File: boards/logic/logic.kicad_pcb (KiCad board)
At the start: 2 copper layers, 48.3 x 76.2 mm, 41 parts, among them IC1 ATTINY85, P1 5V_IN, P2 PROG_CONN, P3 DSPLY_CONN, Q1 Q_NPN_EBC, Q2 Q_NPN_EBC, Q3 Q_NPN_EBC, Q4 Q_NPN_EBC, Q5 Q_NPN_EBC, Q6 Q_NPN_EBC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

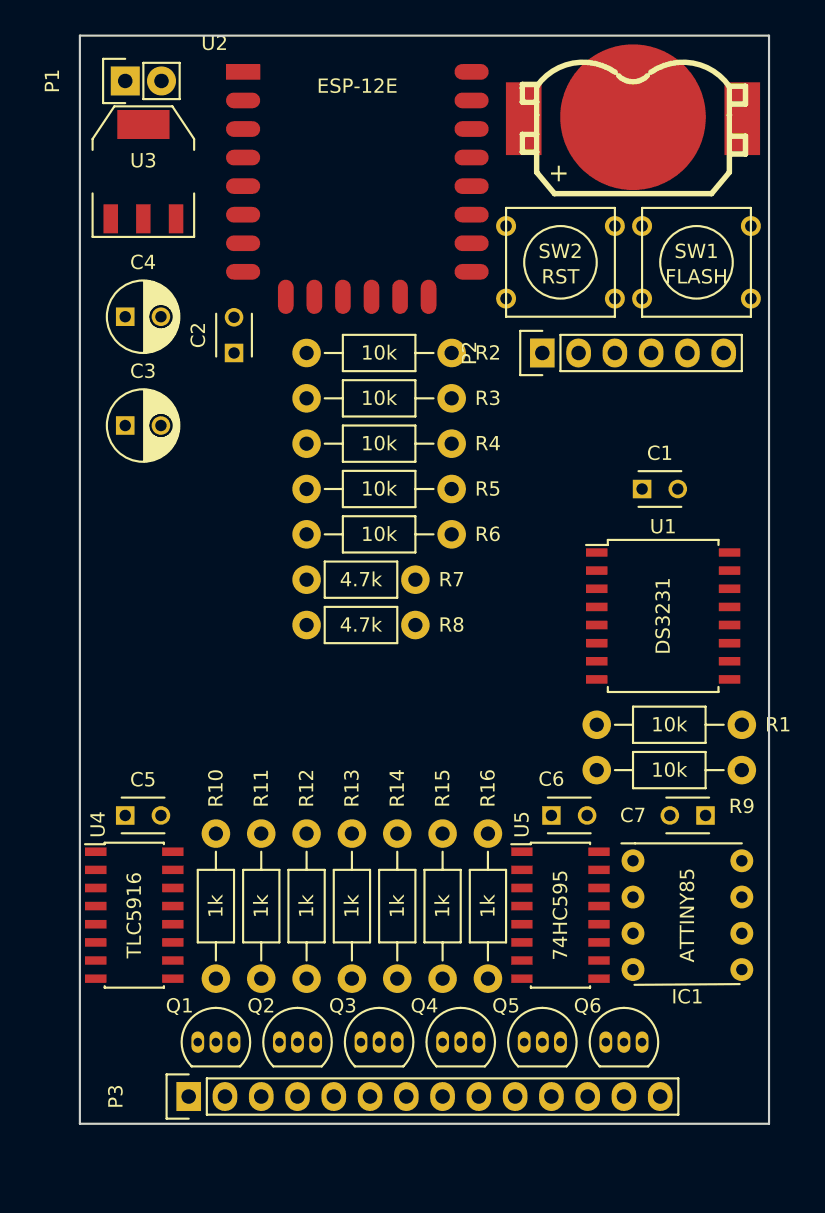
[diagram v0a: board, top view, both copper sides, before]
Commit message: Fit all the components into a smaller board footprint.
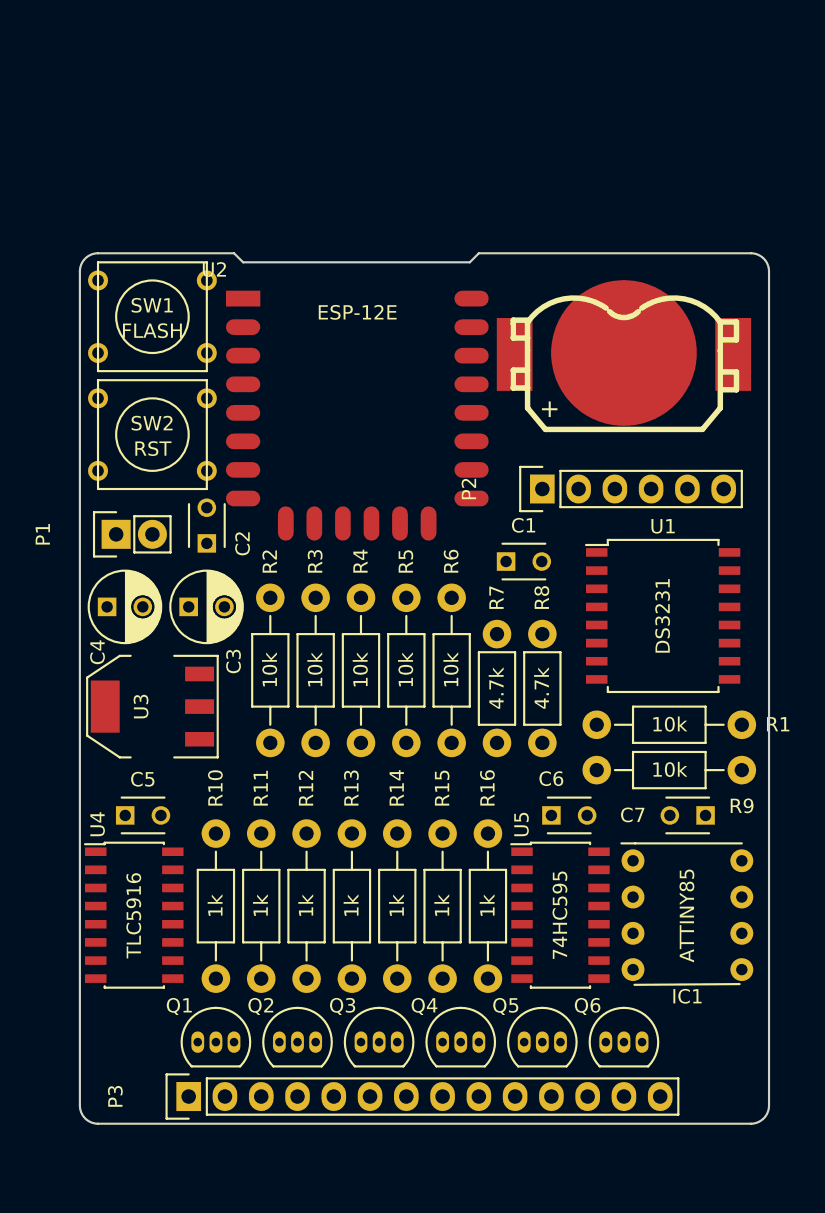
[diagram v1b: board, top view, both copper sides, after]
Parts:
- moved SW1 38.3 mm to (126.4, 87.6)
- moved U3 37.5 mm to (126.4, 114.9), turned to 90 degrees
- moved P1 31.8 mm to (123.8, 102.9)
- moved SW2 31.0 mm to (126.4, 95.9)
- moved R2 27.4 mm to (134.6, 117.5), turned to 90 degrees
- moved R3 24.1 mm to (137.8, 117.5), turned to 90 degrees
- moved R4 21.3 mm to (141.0, 117.5), turned to 90 degrees
- moved C4 20.4 mm to (123.2, 108.0)
- moved R5 19.1 mm to (144.1, 117.5), turned to 90 degrees
- moved R8 18.5 mm to (153.7, 117.5), turned to 90 degrees
- moved R6 17.8 mm to (147.3, 117.5), turned to 90 degrees
- moved R7 17.6 mm to (150.5, 117.5), turned to 90 degrees
- moved BT1 16.5 mm to (159.4, 90.2)
- moved U2 15.9 mm to (132.7, 86.4)
- moved C2 13.5 mm to (130.2, 103.5)
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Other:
- board size 48.3 x 76.2 mm -> 48.3 x 61 mm

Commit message: Switch the LM1117 footprint to SOT-223.
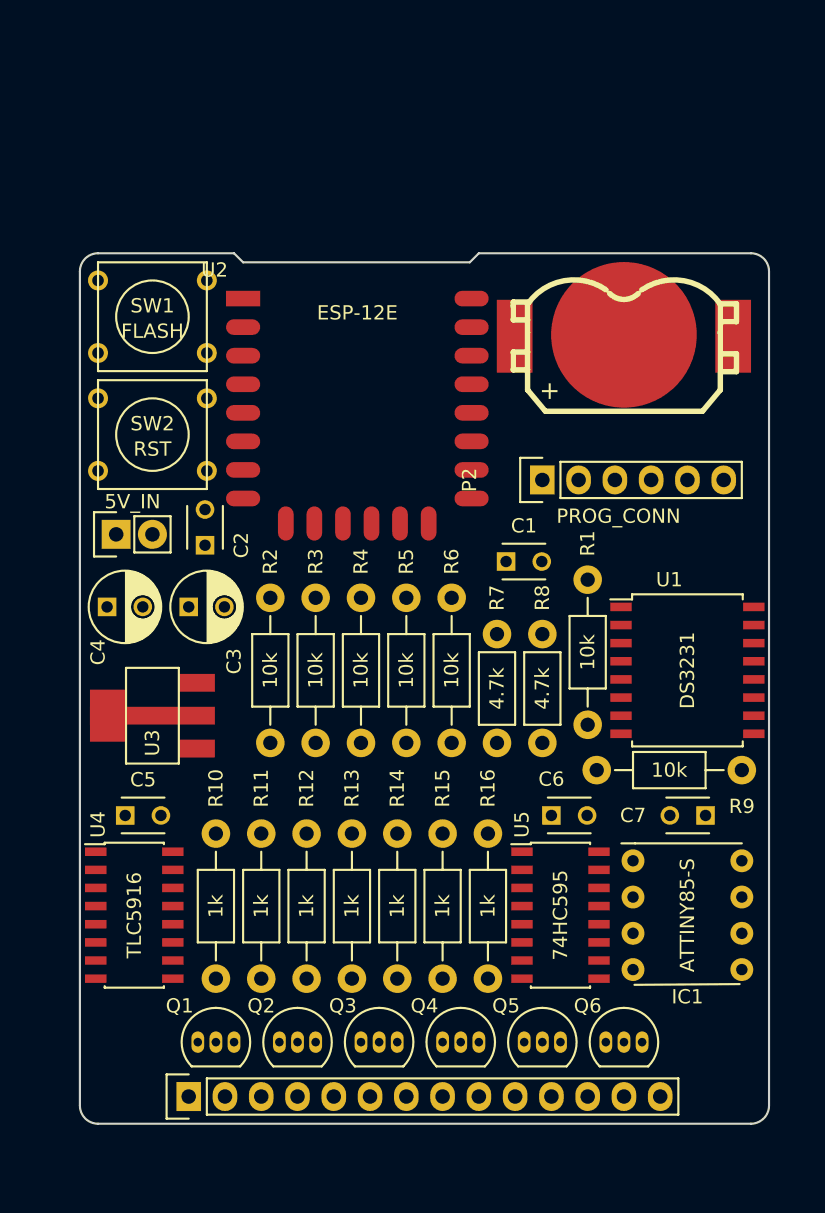
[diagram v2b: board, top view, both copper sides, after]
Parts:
- IC1: value ATTINY85 -> ATTINY85-S
- U3: footprint TO_SOT_Packages_SMD:SOT-223 -> myelin-kicad:SOT-223-LDO-1117LV
- moved U1 4.17 mm to (163.8, 112.4)
- moved BT1 1.27 mm to (159.4, 88.9)
- moved P2 0.63 mm to (153.7, 99.1)
- moved R1 0.63 mm to (156.8, 116.2), turned to 90 degrees
- moved U3 0.63 mm to (126.4, 115.6)
- moved C2 0.18 mm to (130.0, 103.6)

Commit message: Rearrange PCB layout to accomodate mounting screws.
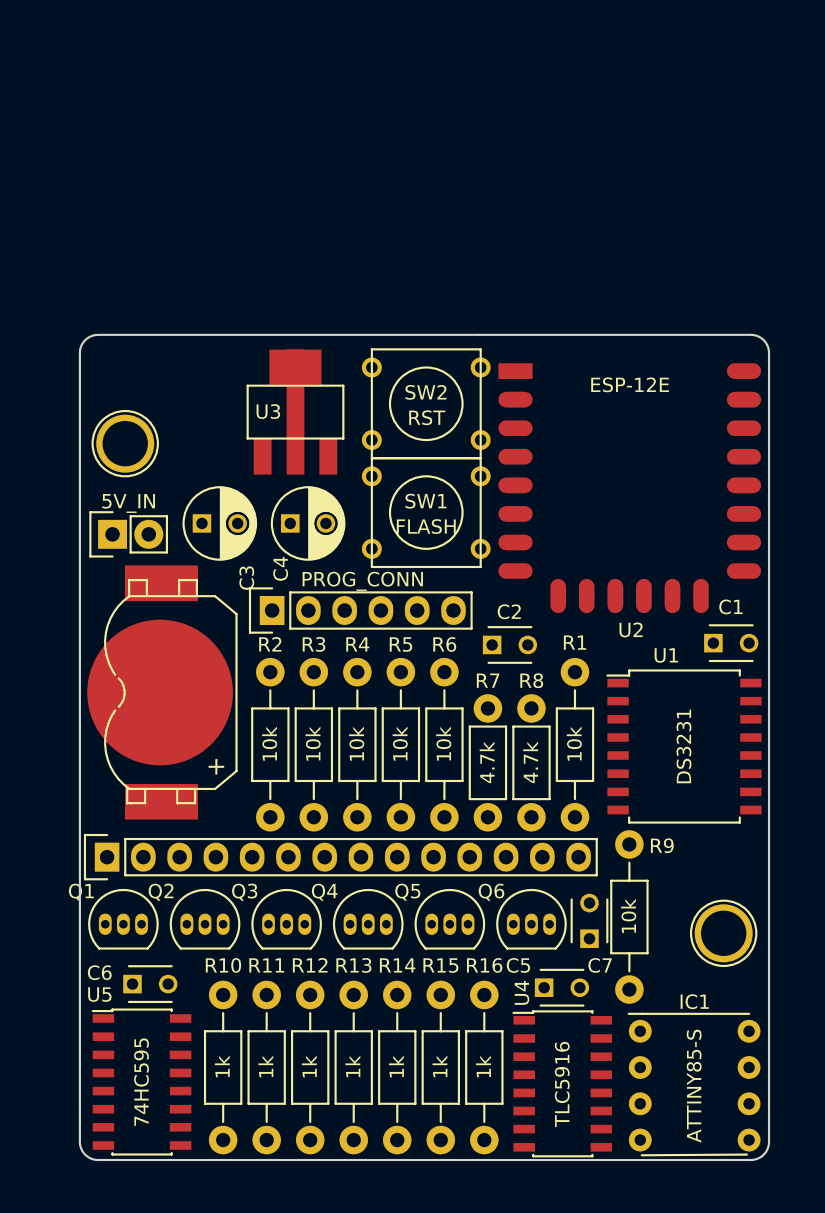
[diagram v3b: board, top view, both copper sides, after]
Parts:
- added REF**: 1pin, Connect:1pin, F.Cu at (166.4, 130.8)
- added REF**: 1pin, Connect:1pin, F.Cu at (124.5, 96.5)
- moved BT1 41.0 mm to (126.9, 113.9), turned to 270 degrees
- moved U4 32.2 mm to (155.1, 141.4)
- moved C5 31.7 mm to (153.8, 134.6)
- moved C6 31.6 mm to (125.0, 134.4)
- moved U5 31.5 mm to (125.6, 141.2)
- moved SW1 23.6 mm to (145.5, 101.3)
- moved U3 23.5 mm to (136.4, 94.3), turned to 0 degrees
- moved C2 21.3 mm to (150.2, 110.6), turned to 0 degrees
- moved P2 21.0 mm to (134.7, 108.2)
- moved U2 19.7 mm to (151.8, 91.4)
- moved SW2 19.3 mm to (145.5, 93.7)
- moved P3 17.7 mm to (123.2, 125.5)
- moved C1 15.6 mm to (165.6, 110.5)
- moved C4 14.1 mm to (136.0, 102.1)
- moved IC1 11.9 mm to (160.5, 137.7)
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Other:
- board size 48.3 x 61 mm -> 48.3 x 57.8 mm

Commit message: Add references for the mounting holes to allow spectra output to work.
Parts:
- renumbered REF** to REF1, REF** to REF2
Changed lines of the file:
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@@
     (links 117)
     (no_connects 116)
-    (area 121.209999 88.824999 169.620001 146.760001)
+    (area 97.104287 47.403566 203.751257 163.830001)
     (thickness 1.6)
     (drawings 29)
@@
     (descr "module 1 pin (ou trou mecanique de percage)")
     (tags DEV)
-    (fp_text reference REF** (at 0 -3.048) (layer F.SilkS) hide
+    (fp_text reference REF1 (at 0 -3.048) (layer F.SilkS) hide
       (effects (font (size 1 1) (thickness 0.15)))
     )
@@
     (descr "module 1 pin (ou trou mecanique de percage)")
     (tags DEV)
-    (fp_text reference REF** (at 0 -3.048) (layer F.SilkS) hide
-      (effects (font (size 1 1) (thickness 0.15)))
-    )
+    (fp_text reference REF2 (at 0 -3.048) (layer F.SilkS) hide
+      (effects (font (size 1 1) (thickness 0.15)))
+    )

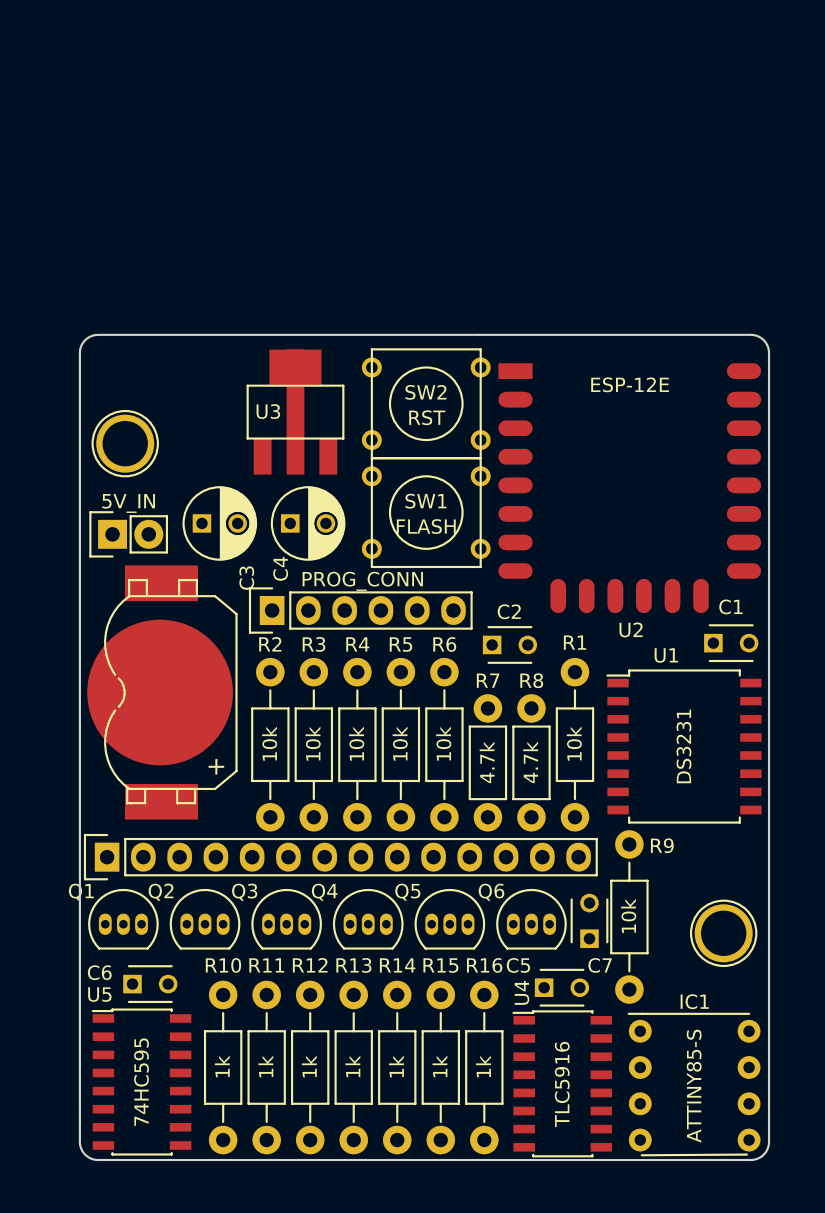
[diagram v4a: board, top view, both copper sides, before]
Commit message: Potential final board layout.
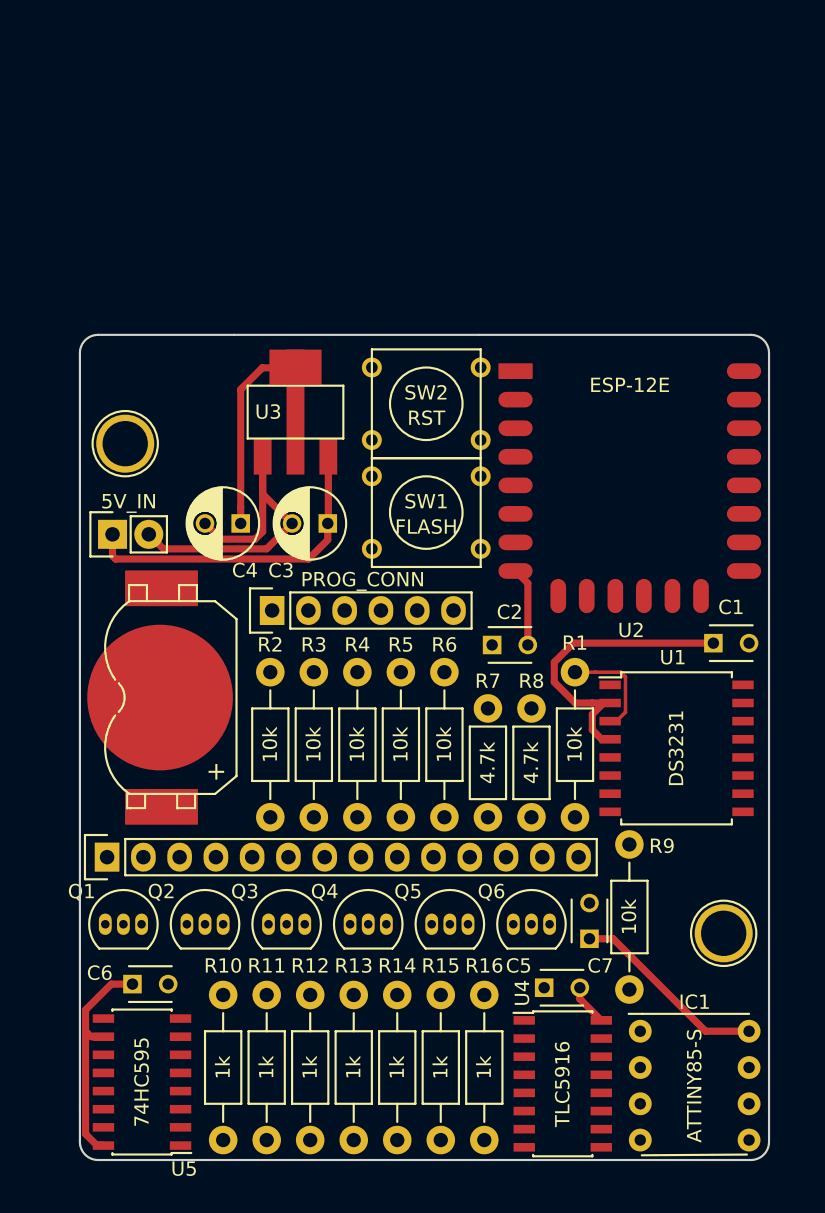
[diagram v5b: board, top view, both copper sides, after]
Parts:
- moved C3 8.81 mm to (138.6, 102.1), turned to 180 degrees
- moved C4 3.47 mm to (132.5, 102.1), turned to 180 degrees
- moved U1 0.57 mm to (163.1, 117.9)
- moved BT1 0.35 mm to (126.9, 114.3)
- turned U5 to 180 degrees
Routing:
- net +3V3: track 0.00 -> 74.6 mm
- net GND: track 0.00 -> 26.7 mm
- net +5V: track 0.00 -> 23.1 mm
- net ESP_GPIO_14: track 0.00 -> 7.48 mm

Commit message: Rearrange silkscreen markers and add TE logo.
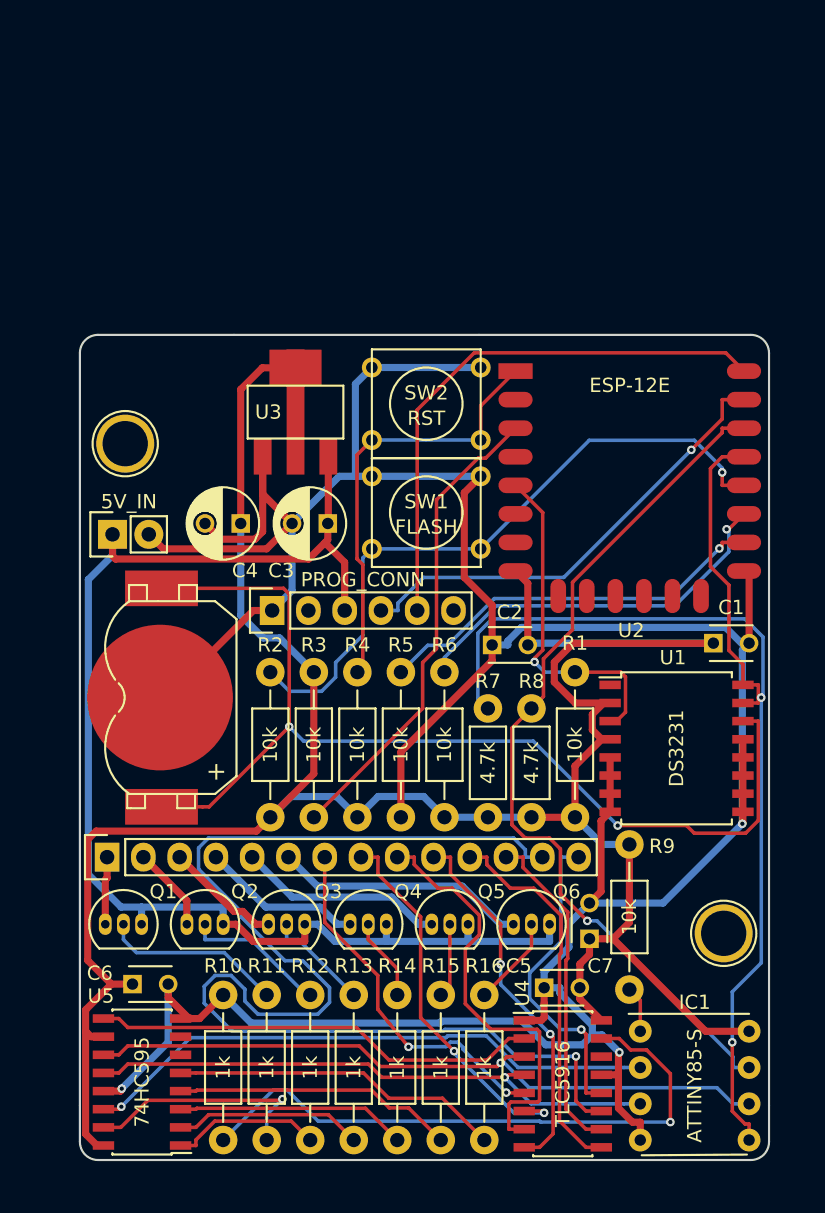
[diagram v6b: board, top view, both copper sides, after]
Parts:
- added G***: LOGO, te_logos:te_22mm_width, B.Cu at (137.7, 117.9)
- added G***: LOGO, te_logos:te_text_22mm_width, B.Cu at (137.3, 114.6)
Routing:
- net GND: track 26.7 -> 239.9 mm, vias 0 -> 3
- net +3V3: track 74.6 -> 184.9 mm
- net SEG_G: track 0.00 -> 85.7 mm, vias 0 -> 1
- net I2C_DATA: track 0.00 -> 85.7 mm, vias 0 -> 2
- net Net-(BT1-Pad1): track 0.00 -> 74.0 mm, vias 0 -> 2
- net +5V: track 23.1 -> 94.4 mm
- net I2C_CLCK: track 0.00 -> 61.3 mm, vias 0 -> 1
- net DISPLAY_SERIAL_CLOCK: track 0.00 -> 49.2 mm, vias 0 -> 1
- net ESP_GPIO_0: track 0.00 -> 46.8 mm, vias 0 -> 1
- net Net-(R10-Pad1): track 0.00 -> 42.9 mm, vias 0 -> 1
- net DISPLAY_SERIAL_DATA: track 0.00 -> 40.6 mm, vias 0 -> 1
- net DISPLAY_SERIAL_LATCH: track 0.00 -> 40.4 mm, vias 0 -> 1
- net CONN_RX: track 0.00 -> 39.1 mm
- net Net-(R3-Pad1): track 0.00 -> 33.4 mm
- net CONN_TX: track 0.00 -> 32.6 mm, vias 0 -> 1
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
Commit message: Add GND pours on the front and back copper layers.
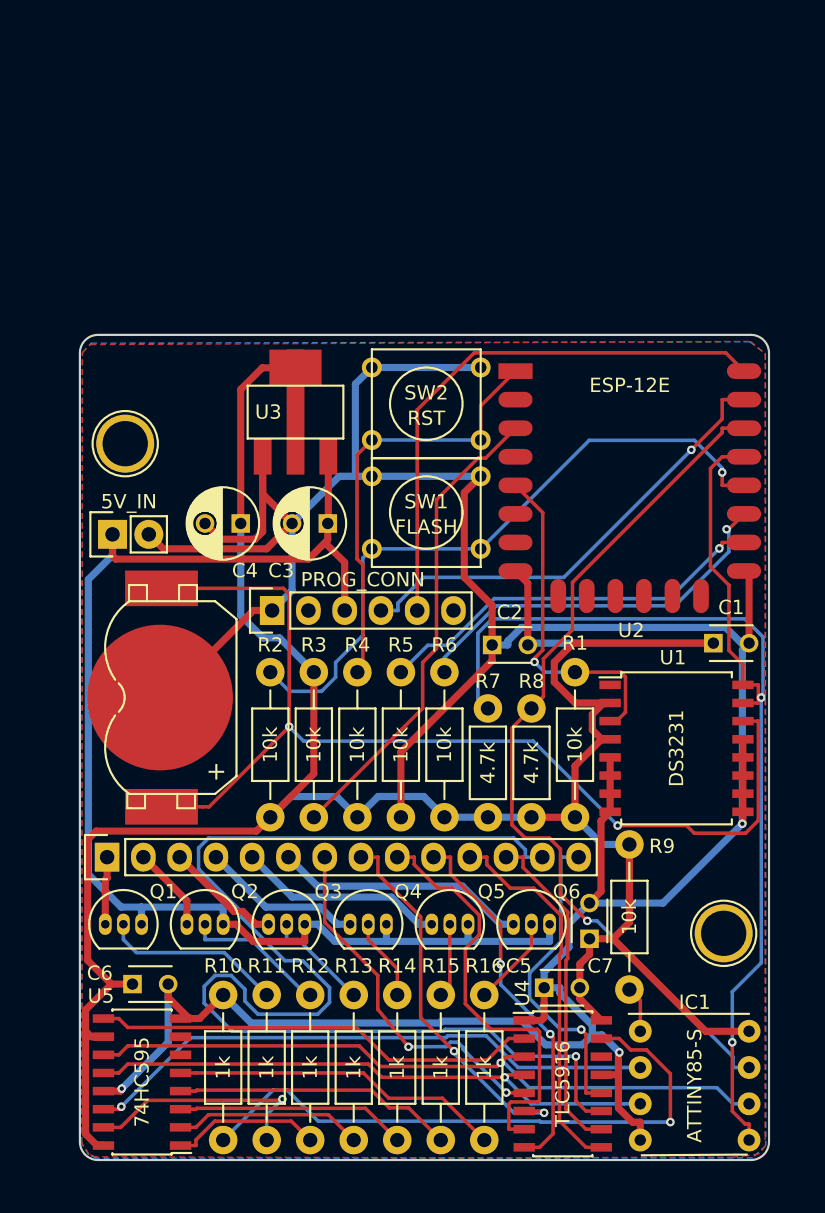
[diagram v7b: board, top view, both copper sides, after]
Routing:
- added copper zone on B.Cu, net GND
- added copper zone on F.Cu, net GND
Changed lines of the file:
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@@
   (layers
     (0 F.Cu signal)
-    (31 B.Cu signal hide)
+    (31 B.Cu signal)
     (32 B.Adhes user)
     (33 F.Adhes user)
@@
       )
     )
+  )
+  (zone (net 2) (net_name GND) (layer F.Cu) (hatch edge 0.508)
+    (connect_pads (clearance 0.508))
+    (min_thickness 0.254)
+    (fill yes (arc_segments 16) (thermal_gap 0.508) (thermal_bridge_width 0.508))
+    (polygon
+      (pts
+        (xy 122.0216 89.5858) (xy 168.2496 89.3572) (xy 169.2656 90.1954) (xy 169.2656 144.8816) (xy 169.291 145.6944)
+        (xy 168.8592 146.2532) (xy 168.0464 146.3802) (xy 167.005 146.4818) (xy 148.1328 146.5326) (xy 122.3772 146.4564)
+        (xy 121.92 146.2786) (xy 121.412 145.4912) (xy 121.4628 90.1446)
+      )
+    )
+  )
+  (zone (net 2) (net_name GND) (layer B.Cu) (hatch edge 0.508)
+    (connect_pads (clearance 0.508))
+    (min_thickness 0.254)
+    (fill yes (arc_segments 16) (thermal_gap 0.508) (thermal_bridge_width 0.508))
+    (polygon
+      (pts
+        (xy 122.0724 89.4842) (xy 168.1988 89.3826) (xy 169.291 90.2208) (xy 169.3164 145.669) (xy 168.402 146.5326)
+        (xy 122.4534 146.558) (xy 121.8946 146.304) (xy 121.412 145.4912) (xy 121.4628 90.1446)
+      )
+    )
